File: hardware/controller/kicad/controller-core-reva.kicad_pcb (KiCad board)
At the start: 2 copper layers, 141.6 x 135.2 mm, 159 parts, among them J101 12V_ISOLATED_INPUT / JST XH, J102 STM_SWD / 1x6 2.54mm, J103 ESP_UART / 1x6 2.54mm, J104 UI_LINK / IDC 2x8 2.54mm, J105 JP13 NTC / 2 vías, J106 JP5 FLOW ADAPTER / VCC-GND-OC, J107 JP14 DOOR / contacto seco, J108 JP16 VISUAL V1..V8 / XH-8, J109 JP22 WATER / RED-WHITE-BLACK, J110 USB-C SERVICE / USB 2.0, J111 USB BENCH POWER / OPEN, J112 24V_ACTUATOR_INPUT / JST XH, J113 JP3 VALVE / JST XH, J114 POWER MONITOR / MEASURE ONLY, J115 JP8 GRINDER / 320VDC, J117 JP24 PUMP / 230VAC, J118 JP17 MAINS / L-N, J121 24V INTERNAL SELECT / OPEN FO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, K701 G5RL-1A-E-TV8 DC24, Q501 SI2308A, Q701 SI2308A / relay coil, U101 STM32G431RBT6, U201 ESP32-S3-WROOM-1U-N8R8, U203 USBLC6-2SC6, U301 AP63203WU-7, U302 TPS22918DBVR, U303 AP63200WU-7 / 24V to 12V, U501 DRV8876PWPR, U502 UCC27517DBVR, U601 TPS3828-33DBVR, U602 SN74LVC2G08DCTR, U603 SN74LVC2G08DCTR

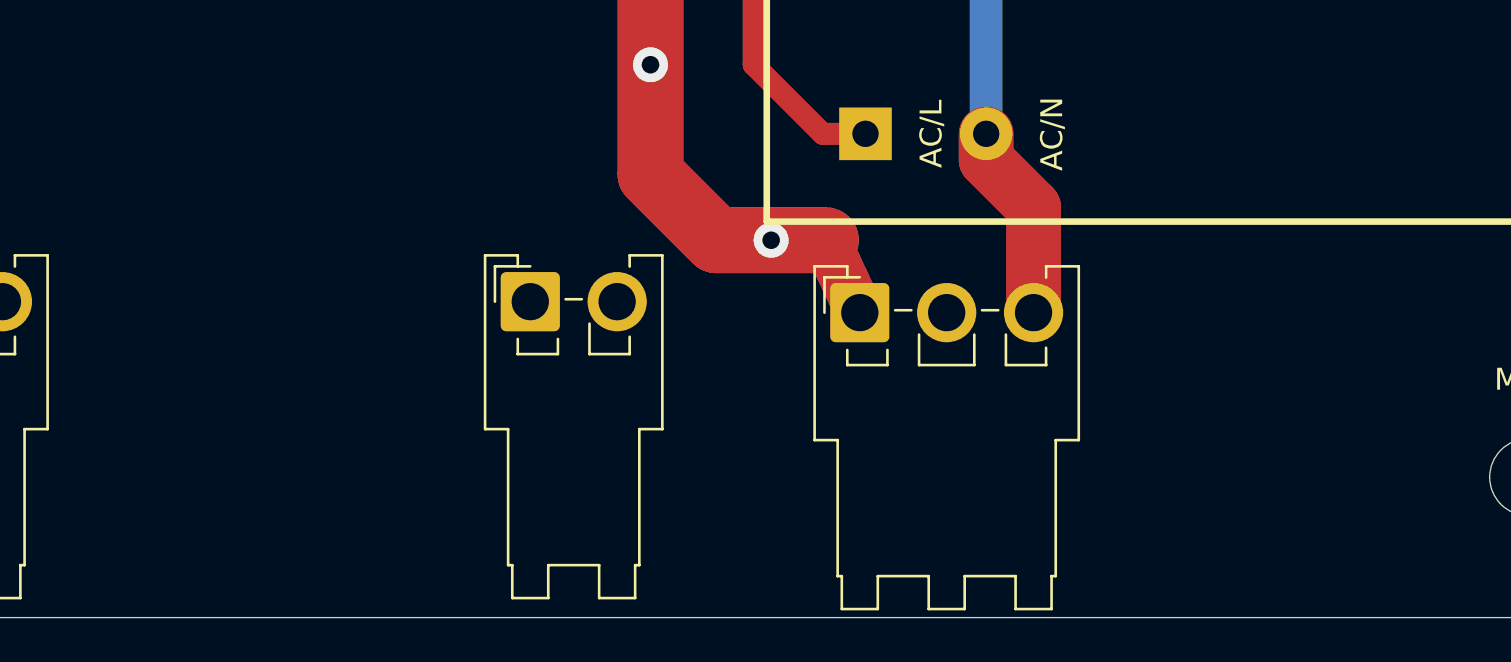
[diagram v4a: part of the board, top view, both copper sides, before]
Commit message: Close JP19, JP1 and JP9 with the owner's measurements
Owner data: only tabs 1 and 3 of JP19 are wired and they are the two ends of
the same boiler element, so their order does not matter. The element measures
27.5 ohm and is rated 1900 W, which is 8.4 A at 230 V, exactly what the doubled
phase copper already carries. JP1 and JP9 are protective-earth tabs, from the
boiler body and the mains inlet.

Draw two footprints: a four-tab FASTON block in a column on 5 mm pitch for the
heater, and a single tab for each earth bond. Both are provisional in their
solder-leg pattern, since the measurements give the tab and the pitch but not
how it lands on the board, so round holes stand in and the note says to check
against a sample.

Tab 3 of JP19 sits nearest the board edge and takes the neutral return, now
routed from JP17 under the connector row and doubled on both layers. Tab 1
waits for the switched live from the triac. The earth bond between JP1 and JP9
is doubled the same way, because it carries fault current until the upstream
protection opens, and PROTECTIVE_EARTH joins the Mains class so it keeps 8 mm
from anything SELV.

All 159 footprints are now placed, the temporary reservation areas are gone and
schematic parity drops from six differences to the three intentional mounting
holes. ERC and DRC clean; 75 connections remain.

Co-Authored-By: Claude Opus 5 <noreply@anthropic.com>
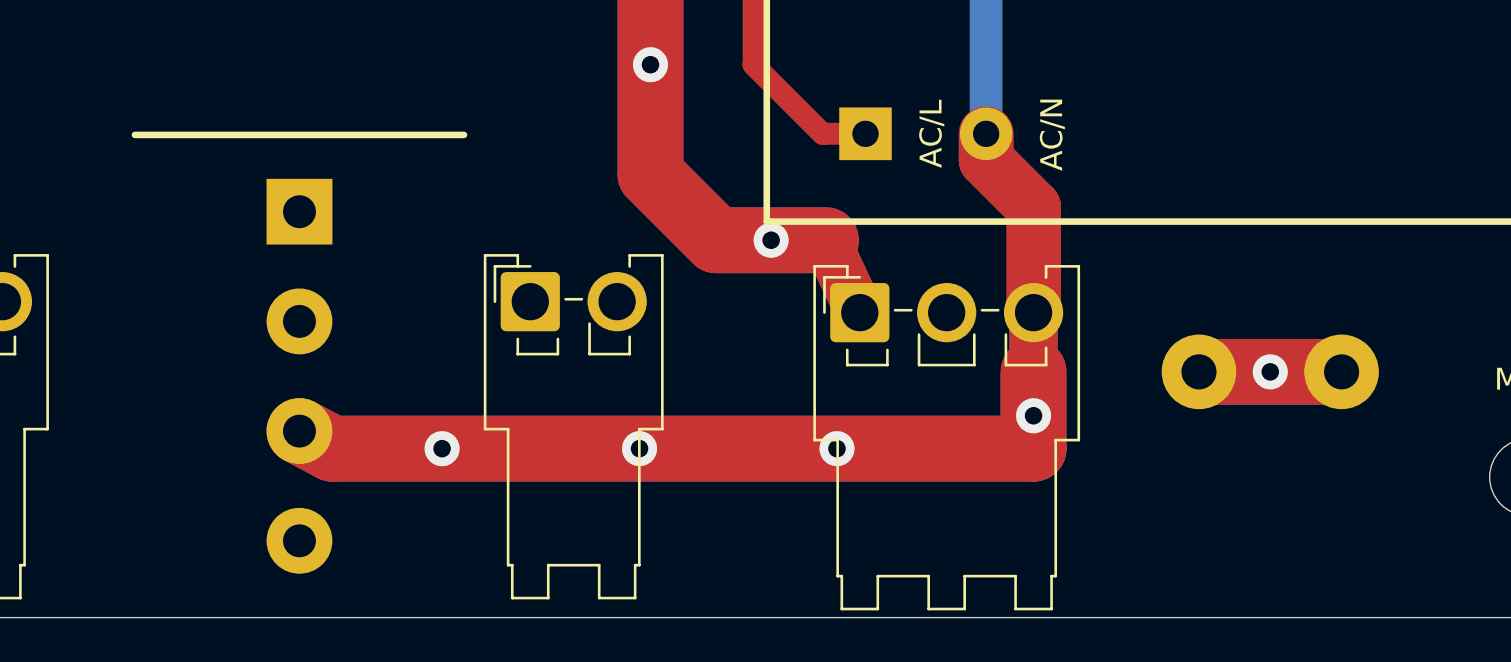
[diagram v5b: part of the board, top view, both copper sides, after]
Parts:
- added J116: JP19 HEATER / 1900W 27R5, OpenSaeco:FASTON_4Tab_6.3x0.8mm_P5.00mm_Column, F.Cu at (80.5, 124.2)
- added J119: JP1 PE TO BOILER, OpenSaeco:FASTON_Tab_6.3x0.8mm_PE, F.Cu at (121.5, 124.0)
- added J120: JP9 PE INPUT, OpenSaeco:FASTON_Tab_6.3x0.8mm_PE, F.Cu at (128.0, 124.0)
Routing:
- net /MAINS_N: track 94.2 -> 174.0 mm, vias 0 -> 4
- net /PROTECTIVE_EARTH: track 0.00 -> 13.0 mm, vias 0 -> 1

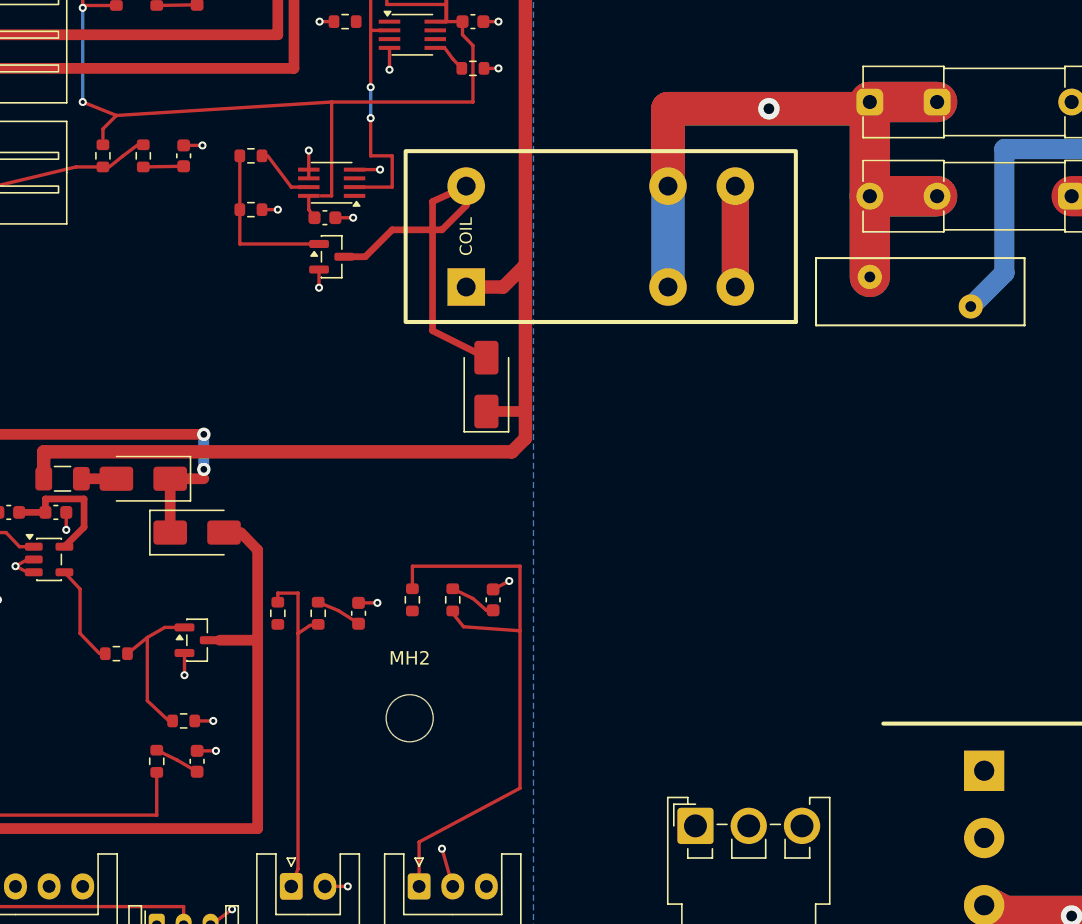
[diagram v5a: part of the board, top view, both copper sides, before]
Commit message: Place and route the heater stage on a 33 mm extruded heatsink
Choose a standard extruded profile, 33 x 21 mm foot and 35 mm tall, at
x = 62-95 mm. It stays at 33 mm rather than the original 40 because the
switched phase has to get from K701 down to the triacs and the only way past is
a 5 mm lane west of the profile. The foot now forbids copper as well as
footprints, since the base sits on the board.

Add the heater stage: MOC3083 straddling the barrier on the standard DIP land
pattern (the long-pad one leaves 7.76 mm between rows, under the 8 mm rule),
BTA24 against the heatsink, R710 in the lane, and an SI2308A driving the LED from
12 V. The spare AND gate in U603 becomes the heater's reset interlock. Gate and
gate feed run on B.Cu, where the mains domain has no plane. Named areas drop the
mains-to-mains clearance to 0.6 mm only on the device pins whose 2.54 mm pitch
the package imposes; the gap between the optocoupler's rows keeps 8 mm.

Still open: PB10 and the interlock to R707, a voltage-rated part for R710, and
the pump stage in the free east half of the profile. ERC and DRC clean.

Co-Authored-By: Claude Opus 5 <noreply@anthropic.com>
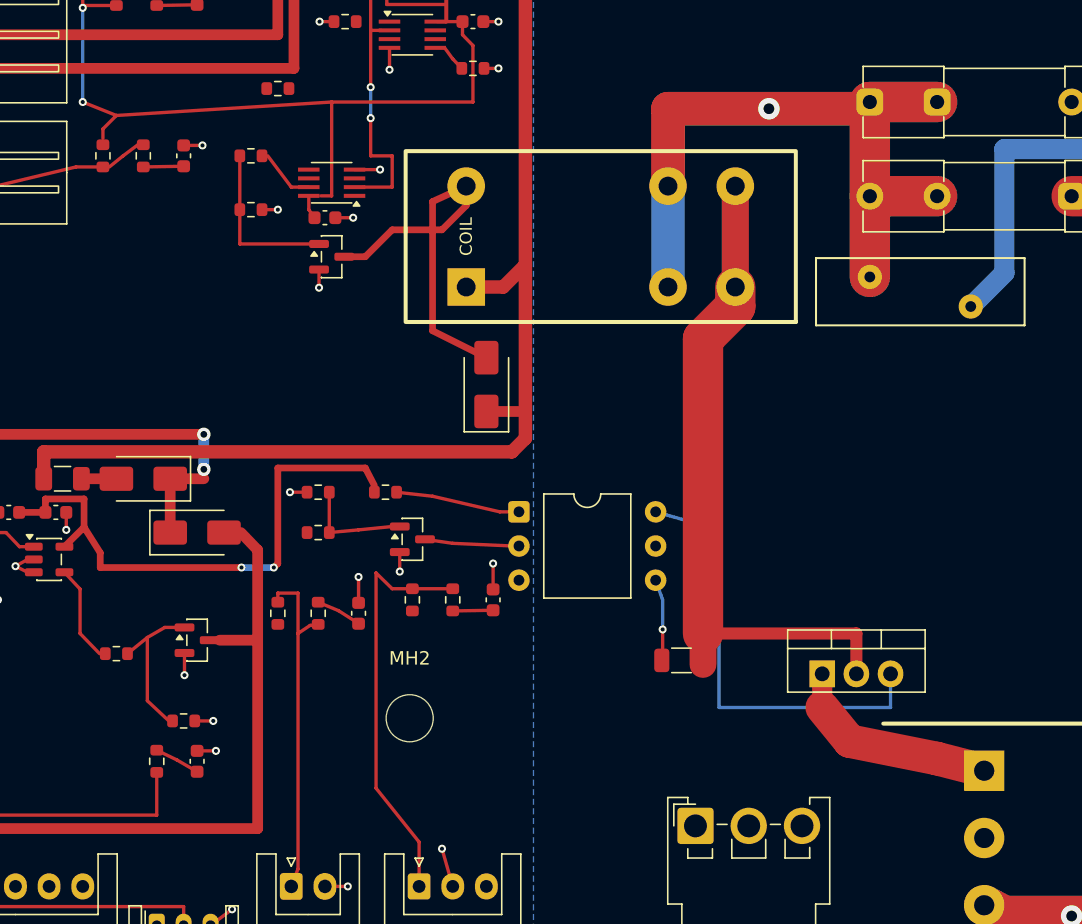
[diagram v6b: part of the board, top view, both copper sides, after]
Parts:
- added Q703: BTA24-800BWRG / heater, Package_TO_SOT_THT:TO-220-3_Vertical, F.Cu at (68.5, 109.5)
- added Q705: SI2308A / heater opto LED, Package_TO_SOT_SMD:SOT-23, F.Cu at (38.0, 99.5)
- added R707: 33 / opto LED gate, Resistor_SMD:R_0603_1608Metric, F.Cu at (31.0, 99.0)
- added R708: 100k / opto LED off, Resistor_SMD:R_0603_1608Metric, F.Cu at (31.0, 96.0)
- added R709: 1k / opto LED series, Resistor_SMD:R_0603_1608Metric, F.Cu at (36.0, 96.0)
- added R710: 470 / gate limit 325Vpk, Resistor_SMD:R_1206_3216Metric, F.Cu at (58.0, 108.5)
- added R711: 10k / heater arm pull-down, Resistor_SMD:R_0603_1608Metric, F.Cu at (28.0, 66.0)
- added U701: MOC3083 / zero-cross, Package_DIP:DIP-6_W10.16mm, F.Cu at (45.9, 97.5)
- turned R404 to -90 degrees
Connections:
- U101 pad 30: unconnected-(U101-PB10-Pad30) -> /HEATER_EN_RAW
- U603 pad 3: unconnected-(U603-2Y-Pad3) -> /HEATER_EN_INTERLOCK
- U603 pad 5: /GND_UI -> /HEATER_EN_RAW
- U603 pad 6: /GND_UI -> /STM_NRST
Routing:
- net /LOAD_L_ENABLED: track 15.0 -> 57.7 mm
- net /HEATER_TRIAC_GATE: track 0.00 -> 32.6 mm
- net /12V_PROTECTED: track 53.4 -> 85.1 mm, vias 0 -> 2
- net /HEATER_AC_SWITCHED: track 0.00 -> 15.3 mm
- net /FLOW_RAW: track 43.2 -> 30.6 mm
- net /HEATER_LED_ANODE: track 0.00 -> 8.82 mm
- net /HEATER_LED_GATE: track 0.00 -> 7.70 mm
- net /HEATER_LED_RETURN: track 0.00 -> 6.59 mm
- net /HEATER_GATE_FEED: track 0.00 -> 5.55 mm, vias 0 -> 1
- net /GND_UI: track 143.0 -> 144.8 mm, vias 87 -> 88

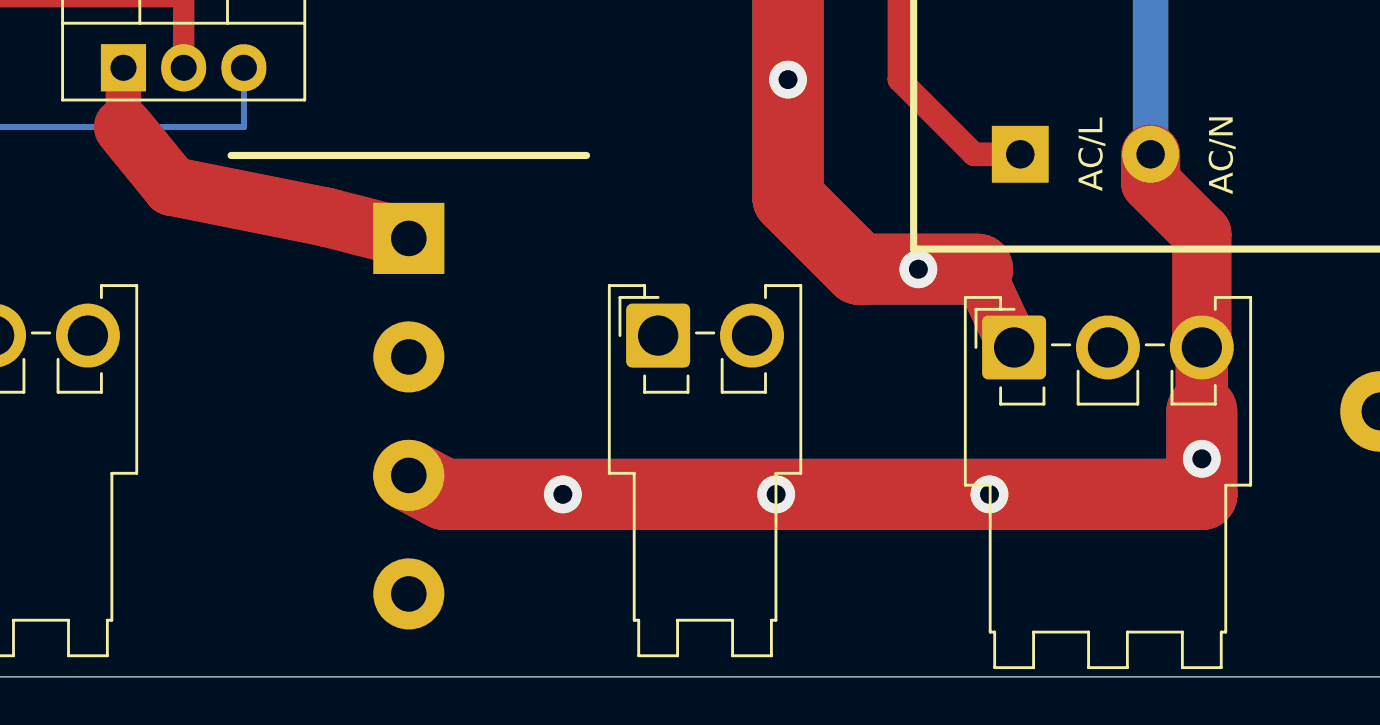
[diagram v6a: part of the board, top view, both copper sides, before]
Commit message: Fit JP19 with the owner-identified TE 1971845-4
The boiler connector is a TE RAST 5 tab header, LCSC C2149727. Its
footprint follows TE drawing C-1971845: two staggered tails per tab in
1.3 mm holes and a 2.5 mm hole for the polarizing post. The housing is
centred to sit flush with the bottom edge, the neutral return climbs
over the post hole, and both tails of every tab are joined.

Co-Authored-By: Claude Opus 5 <noreply@anthropic.com>
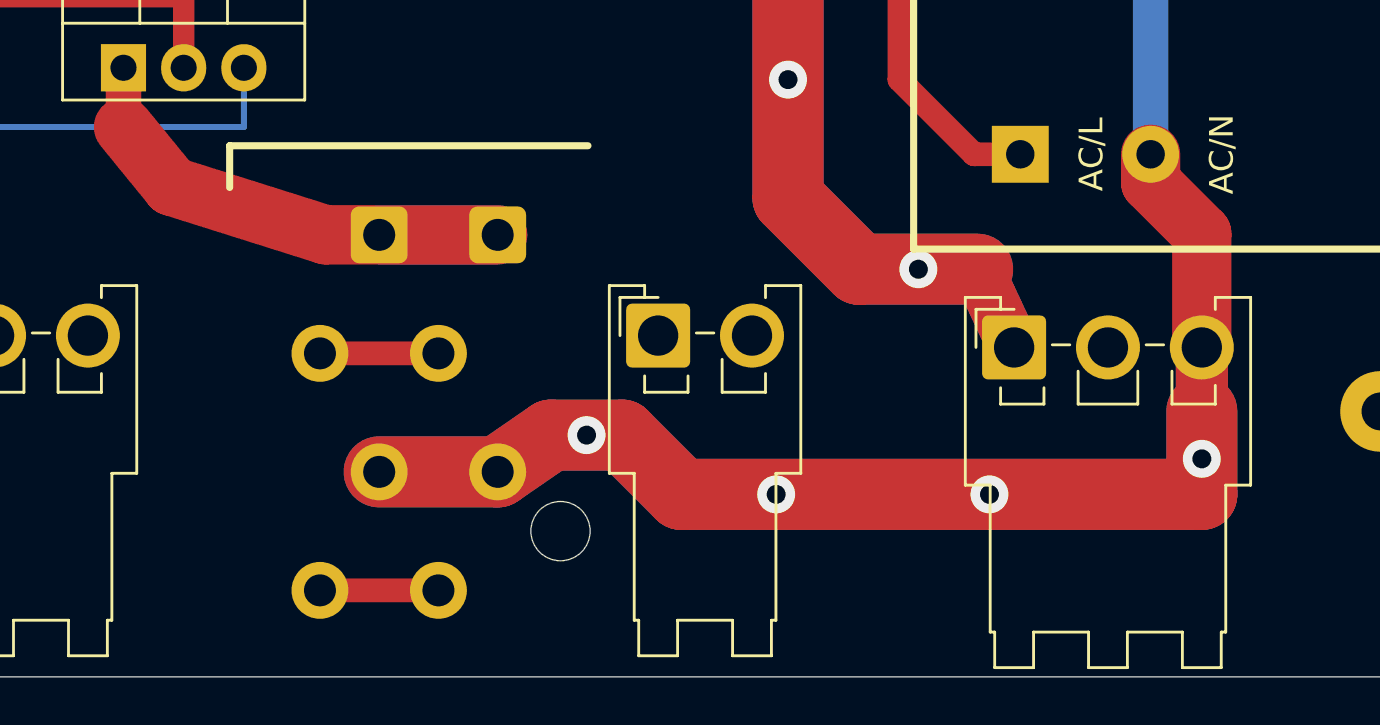
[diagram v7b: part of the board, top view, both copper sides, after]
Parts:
- J116: footprint OpenSaeco:FASTON_4Tab_6.3x0.8mm_P5.00mm_Column -> OpenSaeco:TE_RAST5_1971845-4_1x04_P5.00mm_Vertical
- moved J116 0.15 mm to (80.5, 124.0)
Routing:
- net /HEATER_AC_SWITCHED: track 15.3 -> 24.1 mm
- net /MAINS_N: track 174.0 -> 179.1 mm
- net unconnected-(J116-Pad4): track 0.00 -> 5.00 mm
- net unconnected-(J116-Pad2): track 0.00 -> 5.00 mm

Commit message: Route the heater interlock gate
HEATER_EN_RAW now reaches U603 pin 5 and the R711 pull-down, and the
gated output runs on B.Cu from pin 3 to R707. The reset loop around pin
2 moves east to leave room for that via, and the relay enable runs
straight west first so that pin 6 gets its reset through a via of its
own. Only the PB10 leg from the MCU is left on this chain.

Co-Authored-By: Claude Opus 5 <noreply@anthropic.com>
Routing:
- net /HEATER_EN_INTERLOCK: track 0.00 -> 34.3 mm, vias 0 -> 2
- net /STM_NRST: track 76.4 -> 86.0 mm, vias 6 -> 7
- net /HEATER_EN_RAW: track 0.00 -> 7.29 mm, vias 0 -> 2
- net /MAINS_RELAY_EN: track 4.21 -> 5.21 mm
